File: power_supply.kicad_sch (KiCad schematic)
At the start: 21 parts, among them IC1 MP1584EN, IC2 CH224K, J2 USB4940-00-A

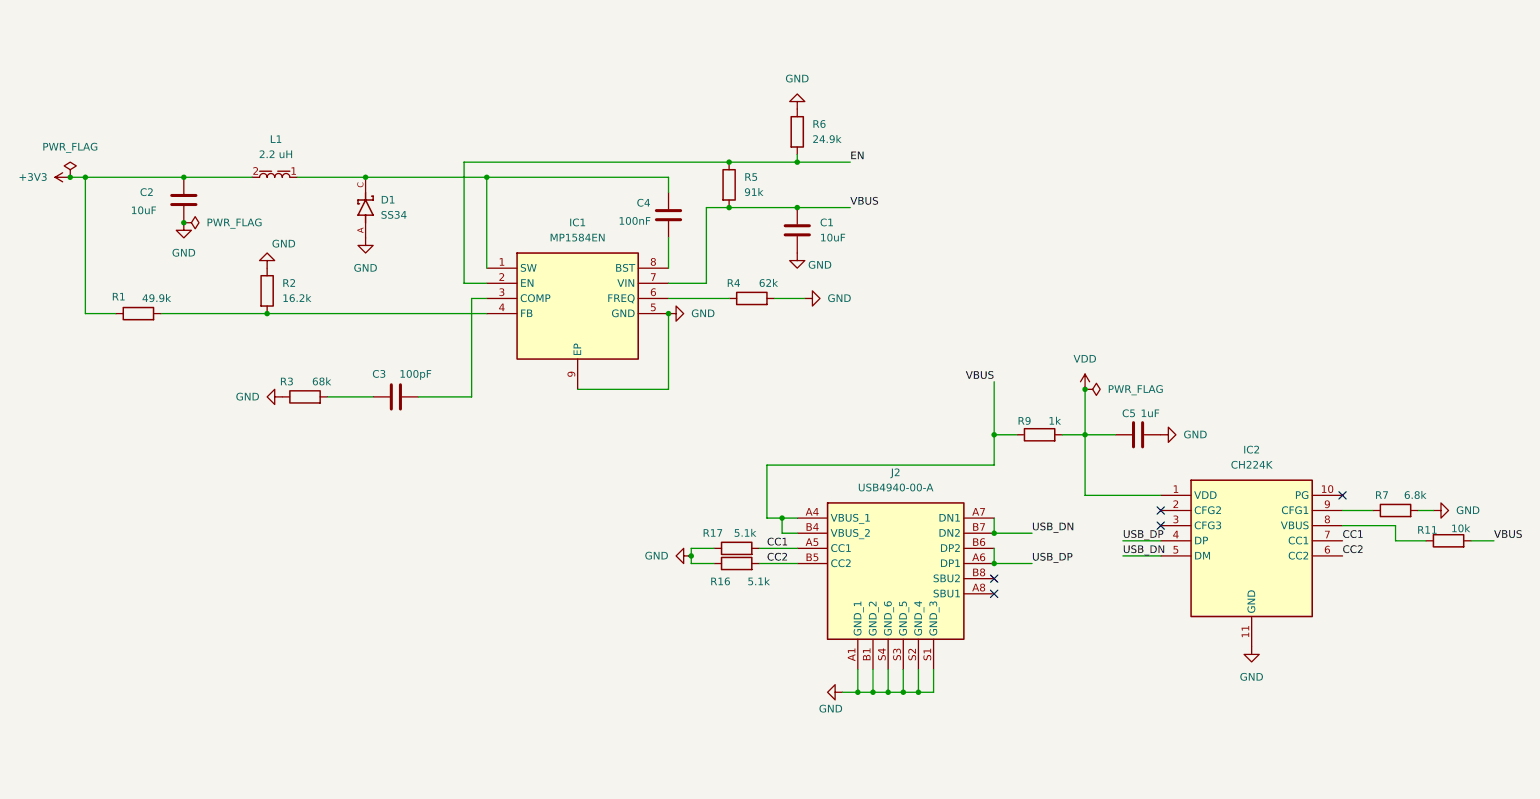
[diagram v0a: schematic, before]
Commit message: improve power delivery schema, improve dac, added oled, encoder, audio out
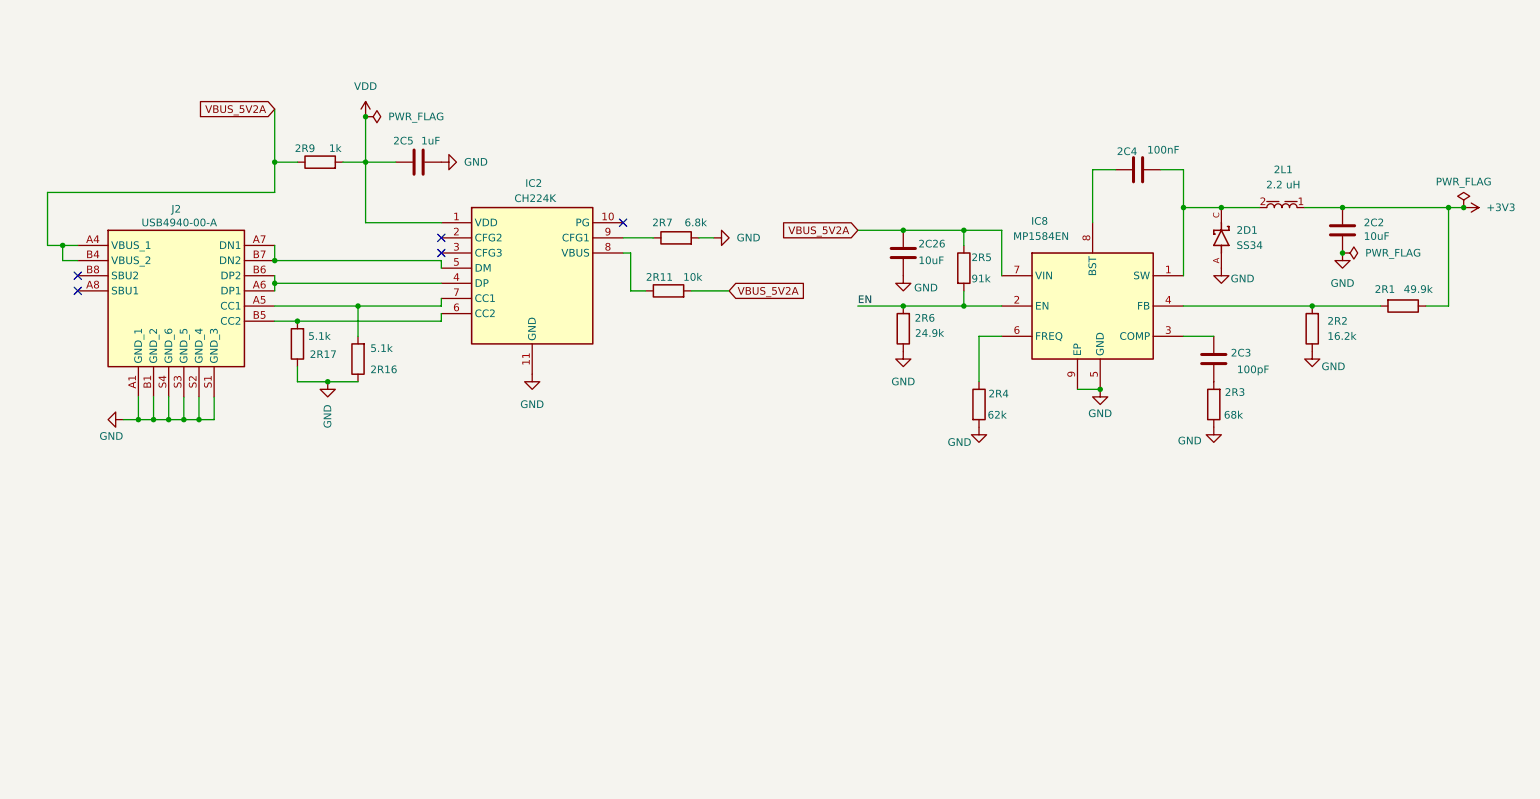
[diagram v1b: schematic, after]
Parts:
- removed C1: 10uF, Capacitor_SMD:C_1206_3216Metric, symbol Device:C
- removed C2: 10uF, Capacitor_SMD:C_0805_2012Metric, symbol Device:C
- removed C3: 100pF, Capacitor_SMD:C_0402_1005Metric, symbol Device:C
- removed C4: 100nF, Capacitor_SMD:C_0402_1005Metric, symbol Device:C
- removed D1: SS34, SS34:DIOM7959X265N, symbol ipradio:SS34
- removed IC1: MP1584EN, SOIC127P600X170-9N, symbol ipradio:MP1584EN
- removed L1: 2.2 uH, Inductor_SMD_Wurth:L_Wurth_WE-LQS-5040, symbol ipradio:5040_74404054022
- removed R1: 49.9k, Resistor_SMD:R_0402_1005Metric, symbol Device:R
- removed R16, R17: 5.1k, Resistor_SMD:R_0402_1005Metric, symbol Device:R
- removed R2: 16.2k, Resistor_SMD:R_0402_1005Metric, symbol Device:R
- removed R3: 68k, Resistor_SMD:R_0402_1005Metric, symbol Device:R
- removed R4: 62k, Resistor_SMD:R_0402_1005Metric, symbol Device:R
- removed R5: 91k, Resistor_SMD:R_0402_1005Metric, symbol Device:R
- removed R6: 24.9k, Resistor_SMD:R_0402_1005Metric, symbol Device:R
- added 2C2: 10uF, Capacitor_SMD:C_0805_2012Metric, symbol Device:C
- added 2C26: 10uF, Capacitor_SMD:C_1206_3216Metric, symbol Device:C
- added 2C3: 100pF, Capacitor_SMD:C_0402_1005Metric, symbol Device:C
- added 2C4: 100nF, Capacitor_SMD:C_0402_1005Metric, symbol Device:C
- added 2D1: SS34, ipradio:DIOM7959X265N, symbol ipradio:SS34
- added 2L1: 2.2 uH, ipradio:L_Wurth_WE-LQS-5040, symbol ipradio:5040_74404054022
- added 2R1: 49.9k, Resistor_SMD:R_0402_1005Metric, symbol Device:R
- added 2R16, 2R17: 5.1k, Resistor_SMD:R_0402_1005Metric, symbol Device:R
- added 2R2: 16.2k, Resistor_SMD:R_0402_1005Metric, symbol Device:R
- added 2R3: 68k, Resistor_SMD:R_0402_1005Metric, symbol Device:R
- added 2R4: 62k, Resistor_SMD:R_0402_1005Metric, symbol Device:R
- added 2R5: 91k, Resistor_SMD:R_0402_1005Metric, symbol Device:R
- added 2R6: 24.9k, Resistor_SMD:R_0402_1005Metric, symbol Device:R
- added IC8: MP1584EN, ipradio:SOIC127P600X170-9N, symbol ipradio:MP1584EN
- IC2: footprint SOP100P600X180-11N -> ipradio:CH224K
- J2: footprint esp32_selfmade:USB494000A -> ipradio:USB494000A
- renumbered C5 to 2C5, R11 to 2R11, R7 to 2R7, R9 to 2R9
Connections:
- net +3V3: now also 2C2.1, 2L1.1, 2R1.1
- net EN: now also 2R5.2, 2R6.2, IC8.2 (EN)
- net GND: now also 2C2.2, 2C26.2, 2D1.A, 2R16.1, 2R17.1, 2R2.1, 2R3.1, 2R4.2, 2R6.1, IC8.5 (GND), IC8.9 (EP)
- net CC1: no longer names the net of IC2.7 (CC1), J2.A5 (CC1)
- net CC1: now also 2R16.2
- net CC2: no longer names the net of IC2.6 (CC2), J2.B5 (CC2)
- net CC2: now also 2R17.2
- net USB_DN: no longer names the net of IC2.5 (DM), J2.A7 (DN1), J2.B7 (DN2)
- net USB_DP: no longer names the net of IC2.4 (DP), J2.A6 (DP1), J2.B6 (DP2)
- net VBUS renamed VBUS_5V2A
- net VBUS_5V2A: now also 2C26.1, 2R5.1, IC8.7 (VIN)
- new net: 2C3.1, 2R3.2
- new net: 2R4.1, IC8.6 (FREQ)
- new net: 2R1.2, 2R2.2, IC8.4 (FB)
- new net: 2C3.2, IC8.3 (COMP)
- new net: 2C4.1, 2D1.C, 2L1.2, IC8.1 (SW)
- new net: 2C4.2, IC8.8 (BST)
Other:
- moved on the sheet: 2C5, 2R11, 2R7, 2R9, IC2, J2

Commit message: finalize power and esp schemas
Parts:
- added 2D2, 2D3: SS34, ipradio:DIOM7959X265N, symbol ipradio:SS34
- 2R1: value 49.9k -> 84.5k
- J2: symbol esp32_selfmade_Esp_32_module:USB4940-00-A -> ipradio:USB4940-00-A
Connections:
- net USB_DP: now reaches J2.A6 (DP1), J2.B6 (DP2)
- net USB_DP: no longer IC2.4 (DP)
- net USB_DN: now reaches J2.A7 (DN1), J2.B7 (DN2)
- net USB_DN: no longer IC2.5 (DM)
- net +3V3: no longer names the net of 2C2.1, 2L1.1, 2R1.1
- net +3V3: now also 2D3.A
- net VBUS_5V2A renamed VBUS_9V
- net VBUS_9V: now also 2D2.A
- new net +5V_BUS: 2D2.C, 2D3.C
- no-connect marks 5 -> 7
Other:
- moved on the sheet: 2C2, 2C26, 2C3, 2C4, 2C5, 2D1, 2L1, 2R1, 2R11, 2R16, 2R17, 2R2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

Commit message: finalized schema
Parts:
- removed 2C5: 1uF, Capacitor_SMD:C_0402_1005Metric, symbol Device:C
- removed 2D2, 2D3: SS34, ipradio:DIOM7959X265N, symbol ipradio:SS34
- removed 2R9: 1k, Resistor_SMD:R_0402_1005Metric, symbol Device:R
- added 2C27: 1uF, Capacitor_SMD:C_1206_3216Metric, symbol Device:C
- added 2C28: 100nF, Capacitor_SMD:C_1206_3216Metric, symbol Device:C
- added 2C29: 10uF, Capacitor_SMD:C_1206_3216Metric, symbol Device:C
- added 2C6: 10uF, Capacitor_SMD:C_0805_2012Metric, symbol Device:C
- added 2C7: 1uF, Capacitor_SMD:C_0805_2012Metric, symbol Device:C
- added 2C8: 100nF, Capacitor_SMD:C_0805_2012Metric, symbol Device:C
- added 2D2, 2D3: D_TVS, Diode_SMD:D_SOD-123, symbol Device:D_TVS
- added 2R12: 10k, Resistor_SMD:R_0402_1005Metric, symbol Device:R
- 2R11: value 10k -> 1k
- 2R5: value 91k -> 100k
- 2R6: value 24.9k -> 24k
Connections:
- net GND: now also 2R7.1, 2C27.2, 2C28.2, 2C29.2, 2C6.2, 2C7.2, 2C8.2, 2D2.1 (A1), 2D3.1 (A1); no longer 2R7.2
- net CC1: now reaches 2R16.2, IC2.7 (CC1), J2.A5 (CC1)
- net CC1: now also 2D2.2 (A2)
- net CC2: now reaches 2R17.2, IC2.6 (CC2), J2.B5 (CC2)
- net CC2: now also 2D3.2 (A2)
- net V_SYS_5V2A: now reaches 2C2.1, 2L1.1, 2R1.1
- net V_SYS_5V2A: now also 2C6.1, 2C7.1, 2C8.1
- net at IC2.8 (VBUS): now also 2R12.2; no longer 2R11.1
- net at IC2.9 (CFG1): now also 2R7.2; no longer 2R7.1
- net EN: no longer names the net of 2R5.2, IC8.2 (EN)
- net EN: no longer 2R6.2
- net VBUS_9V renamed VBUS_5V3A_9V1.5A
- net VBUS_5V3A_9V1.5A: now also 2R11.1, 2R6.2, 2C27.1, 2C28.1, 2C29.1, 2R12.1; no longer 2R11.2
- net VDD: no longer names the net of IC2.1 (VDD)
- net VDD: now also 2R11.2
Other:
- moved on the sheet: 2C2, 2C26, 2C3, 2C4, 2D1, 2L1, 2R1, 2R16, 2R17, 2R2, 2R3, 2R4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
